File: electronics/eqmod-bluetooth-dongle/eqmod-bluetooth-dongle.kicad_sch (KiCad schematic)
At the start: 6 parts, among them J1 Mount

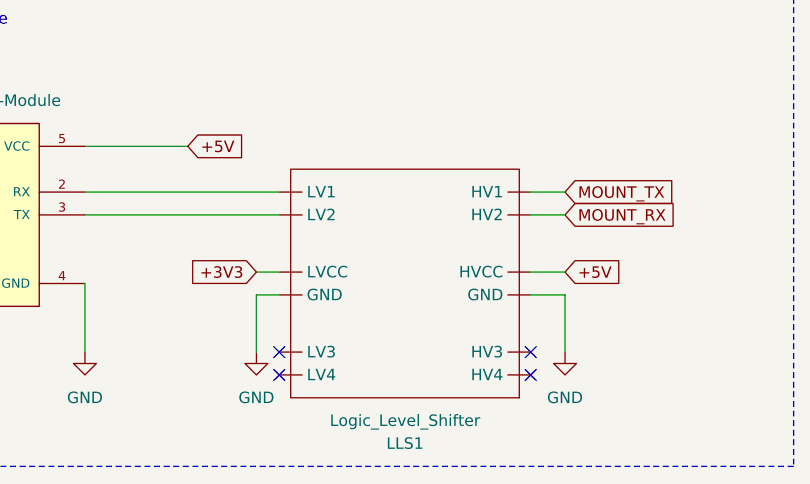
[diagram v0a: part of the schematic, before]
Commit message: feat: Initiate PCB layout (#3)
* Init PCB layout

* With power planes

* With markings

* Documenting PCB layout 

* First test ready
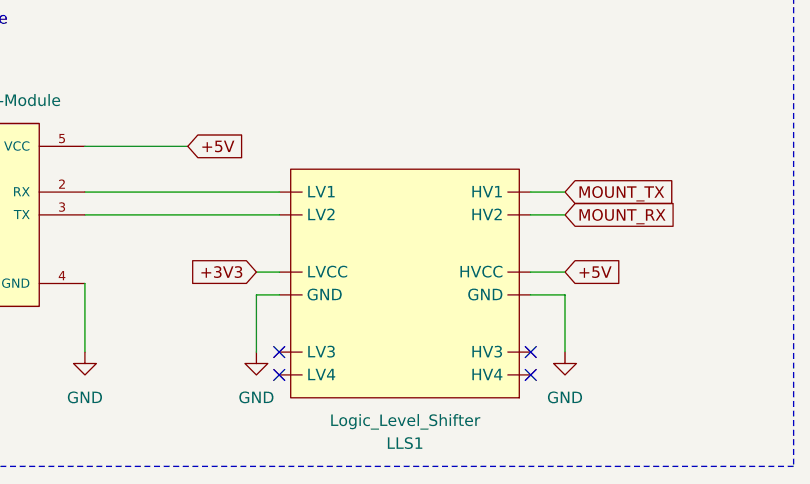
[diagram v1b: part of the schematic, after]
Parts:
- LLS1: footprint Soldered_Logic_Level_Shifter:Logic Level Shifter -> Soldered_Logic_Level_Shifter:333029_Logic_Level_Shifter
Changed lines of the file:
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@@
 			)
 		)
-		(property "Footprint" "Soldered_Logic_Level_Shifter:Logic Level Shifter"
+		(property "Footprint" "Soldered_Logic_Level_Shifter:333029_Logic_Level_Shifter"
 			(at 88.9 104.14 0)
 			(effects

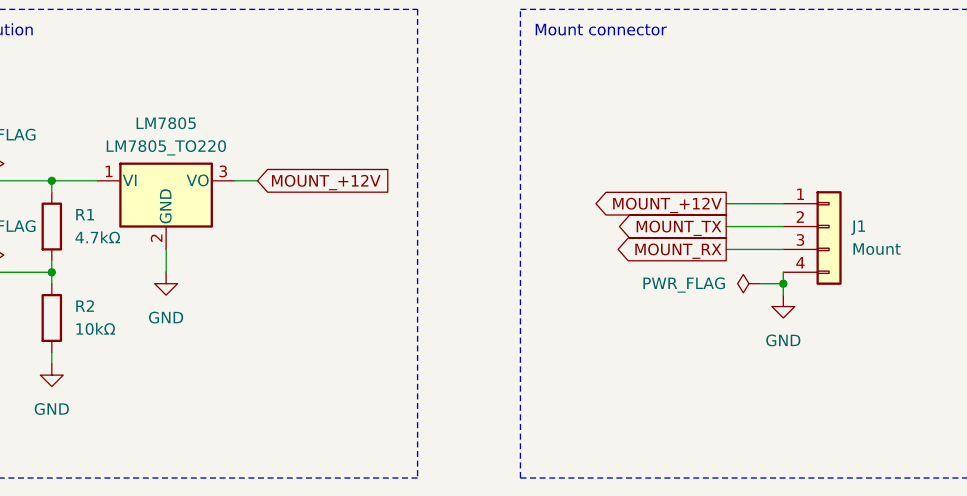
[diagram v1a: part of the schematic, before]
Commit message: Change mount connector to standard JST connector
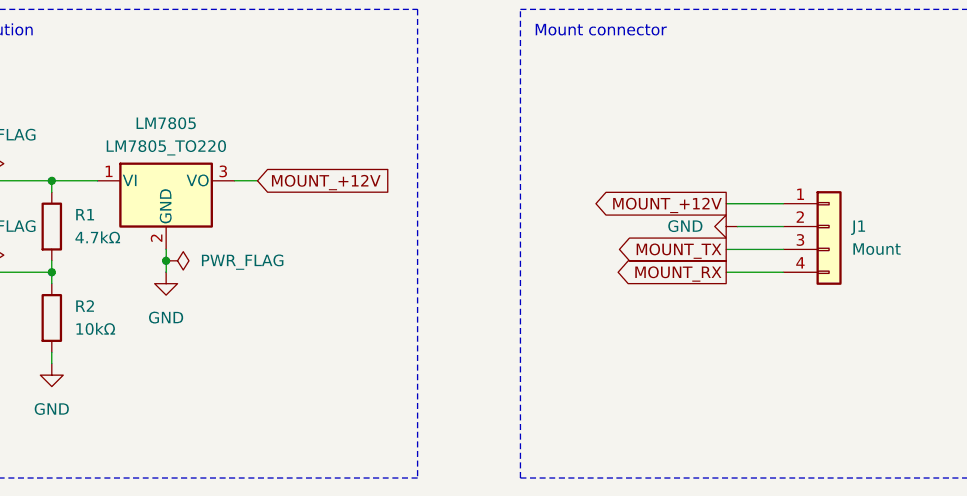
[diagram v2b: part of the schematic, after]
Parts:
- J1: footprint Connector_PinHeader_2.54mm:PinHeader_1x04_P2.54mm_Vertical -> Connector_JST:JST_PH_B4B-PH-K_1x04_P2.00mm_Vertical
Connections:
- net GND: now also J1.2 (Pin_2); no longer J1.4 (Pin_4)
- net MOUNT_RX: now also J1.4 (Pin_4); no longer J1.3 (Pin_3)
- net MOUNT_TX: now also J1.3 (Pin_3); no longer J1.2 (Pin_2)
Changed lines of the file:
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@@
+	)
+	(junction
+		(at 180.34 86.36)
+		(diameter 0)
+		(color 0 0 0 0)
 	)
 	(junction
@@
 	)
 	(junction
-		(at 248.92 88.9)
-		(diameter 0)
-		(color 0 0 0 0)
-	)
-	(junction
 		(at 167.64 77.47)
 		(diameter 0)
@@
 	(wire
 		(pts
+			(xy 242.57 85.09) (xy 248.92 85.09)
+		)
+		(stroke
+			(width 0)
+			(type default)
+		)
+	)
+	(wire
+		(pts
 			(xy 167.64 86.36) (xy 167.64 87.63)
 		)
@@
 	(wire
 		(pts
-			(xy 242.57 82.55) (xy 248.92 82.55)
-		)
-		(stroke
-			(width 0)
-			(type default)
-		)
-	)
-	(wire
-		(pts
-			(xy 248.92 88.9) (xy 248.92 90.17)
-		)
-		(stroke
-			(width 0)
-			(type default)
-		)
-	)
-	(wire
-		(pts
-			(xy 246.38 88.9) (xy 248.92 88.9)
+			(xy 243.84 82.55) (xy 248.92 82.55)
+		)
+		(stroke
+			(width 0)
+			(type default)
+		)
+	)
+	(wire
+		(pts
+			(xy 180.34 86.36) (xy 180.34 87.63)
 		)
 		(stroke
@@
 	(wire
 		(pts
+			(xy 242.57 87.63) (xy 248.92 87.63)
+		)
+		(stroke
+			(width 0)
+			(type default)
+		)
+	)
+	(wire
+		(pts
 			(xy 72.39 88.9) (xy 74.93 88.9)
 		)
@@
 	(wire
 		(pts
-			(xy 242.57 85.09) (xy 248.92 85.09)
-		)
-		(stroke
-			(width 0)
-			(type default)
-		)
-	)
-	(wire
-		(pts
 			(xy 102.87 82.55) (xy 106.68 82.55)
 		)
@@
 	(wire
 		(pts
-			(xy 248.92 87.63) (xy 248.92 88.9)
-		)
-		(stroke
-			(width 0)
-			(type default)
-		)
-	)
-	(wire
-		(pts
 			(xy 53.34 74.93) (xy 64.77 74.93)
 		)
@@
 	(wire
 		(pts
-			(xy 180.34 85.09) (xy 180.34 87.63)
+			(xy 180.34 85.09) (xy 180.34 86.36)
 		)
 		(stroke
@@
 	(global_label "MOUNT_RX"
 		(shape output)
-		(at 242.57 85.09 180)
+		(at 242.57 87.63 180)
 		(fields_autoplaced yes)
 		(effects
@@
 		)
 		(property "Intersheetrefs" "${INTERSHEET_REFS}"
-			(at 229.7272 85.09 0)
+			(at 229.7272 87.63 0)
 			(effects
 				(font
@@
 	(global_label "MOUNT_TX"
 		(shape output)
-		(at 242.57 82.55 180)
+		(at 242.57 85.09 180)
 		(fields_autoplaced yes)
 		(effects
@@
 		)
 		(property "Intersheetrefs" "${INTERSHEET_REFS}"
-			(at 230.0296 82.55 0)
+			(at 230.0296 85.09 0)
 			(effects
 				(font
@@
 	(symbol
 		(lib_id "power:GND")
-		(at 248.92 90.17 0)
+		(at 243.84 82.55 270)
 		(unit 1)
 		(exclude_from_sim no)
@@
 		(fields_autoplaced yes)
 		(property "Reference" "#PWR06"
-			(at 248.92 96.52 0)
+			(at 237.49 82.55 0)
 			(effects
 				(font
@@
 		)
 		(property "Value" "GND"
-			(at 248.92 95.25 0)
-			(effects
-				(font
-					(size 1.27 1.27)
-				)
+			(at 240.03 82.5499 90)
+			(effects
+				(font
+					(size 1.27 1.27)
+				)
+				(justify right)
 			)
 		)
 		(property "Footprint" ""
-			(at 248.92 90.17 0)
+			(at 243.84 82.55 0)
 			(effects
 				(font
@@
 		)
 		(property "Datasheet" ""
-			(at 248.92 90.17 0)
+			(at 243.84 82.55 0)
 			(effects
 				(font
@@
 		)
 		(property "Description" "Power symbol creates a global label with name \"GND\" , ground"
-			(at 248.92 90.17 0)
+			(at 243.84 82.55 0)
 			(effects
 				(font
@@
 			)
 		)
-		(property "Footprint" "Connector_PinHeader_2.54mm:PinHeader_1x04_P2.54mm_Vertical"
+		(property "Footprint" "Connector_JST:JST_PH_B4B-PH-K_1x04_P2.00mm_Vertical"
 			(at 254 82.55 0)
 			(effects
@@
 	(symbol
 		(lib_id "power:PWR_FLAG")
-		(at 246.38 88.9 90)
+		(at 180.34 86.36 270)
 		(unit 1)
 		(exclude_from_sim no)
@@
 		(on_board yes)
 		(dnp no)
-		(fields_autoplaced yes)
 		(property "Reference" "#FLG02"
-			(at 244.475 88.9 0)
+			(at 182.245 86.36 0)
 			(effects
 				(font
@@
 		)
 		(property "Value" "PWR_FLAG"
-			(at 242.57 88.8999 90)
+			(at 184.15 86.3601 90)
 			(effects
 				(font
@@
 		)
 		(property "Footprint" ""
-			(at 246.38 88.9 0)
+			(at 180.34 86.36 0)
 			(effects
 				(font
@@
 		)
 		(property "Datasheet" "~"
-			(at 246.38 88.9 0)
+			(at 180.34 86.36 0)
 			(effects
 				(font
@@
 		)
 		(property "Description" "Special symbol for telling ERC where power comes from"
-			(at 246.38 88.9 0)
-			(effects
-				(font
+			(at 180.34 86.36 0)
+			(effects
+				(font

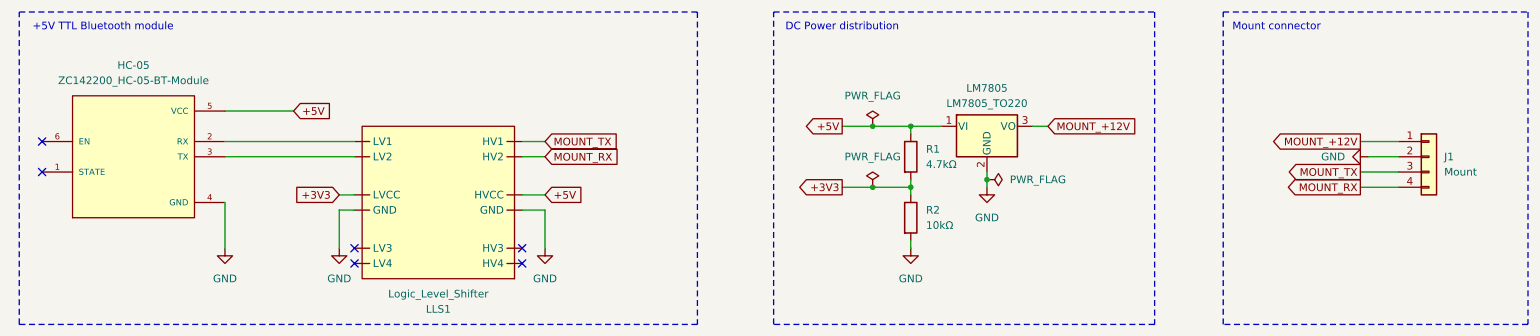
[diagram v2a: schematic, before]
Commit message: Fix: Use connector that can be sourced from supplier (#6)
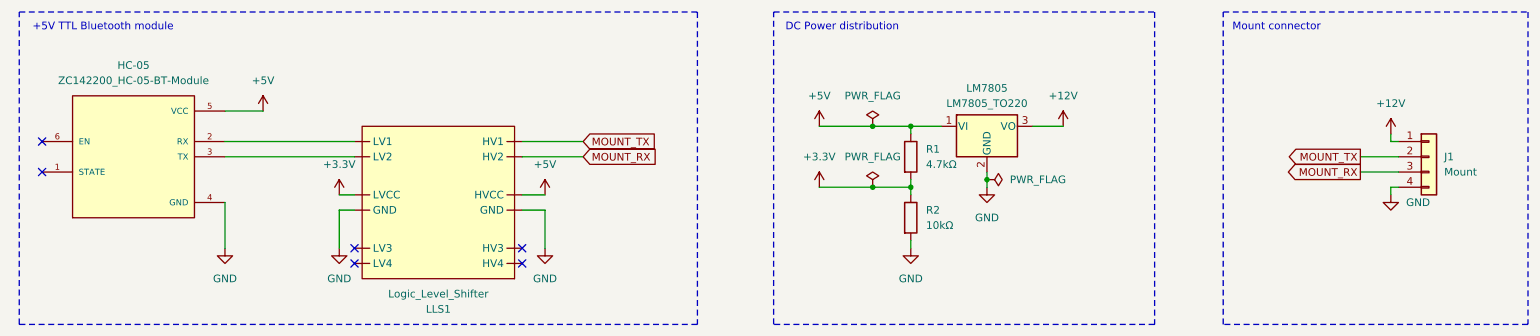
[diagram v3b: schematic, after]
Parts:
- J1: footprint Connector_JST:JST_PH_B4B-PH-K_1x04_P2.00mm_Vertical -> Connector_JST:JST_XH_B4B-XH-A_1x04_P2.50mm_Vertical
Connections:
- net GND: now also J1.4 (Pin_4); no longer J1.2 (Pin_2)
- net MOUNT_RX: now also J1.3 (Pin_3); no longer J1.4 (Pin_4)
- net MOUNT_TX: now also J1.2 (Pin_2); no longer J1.3 (Pin_3)
- net +3V3 renamed +3.3V
- net MOUNT_+12V renamed +12V
